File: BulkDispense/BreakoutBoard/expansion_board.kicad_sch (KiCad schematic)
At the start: 10 parts, among them J24 Waste 2/2 Media Valve Power, J25 Waste 2/2 Media Valve GND, J26 Waste Line Sensor 1, J27 Waste Line Sensor 2, J28 Waste Bottle Sensor 1, J29 Waste Bottle Sensor 2, J30 Waste 3/2 Media Valve, J31 Waste Vacuum Sensor 1, J32 Waste Vacuum Sensor 2

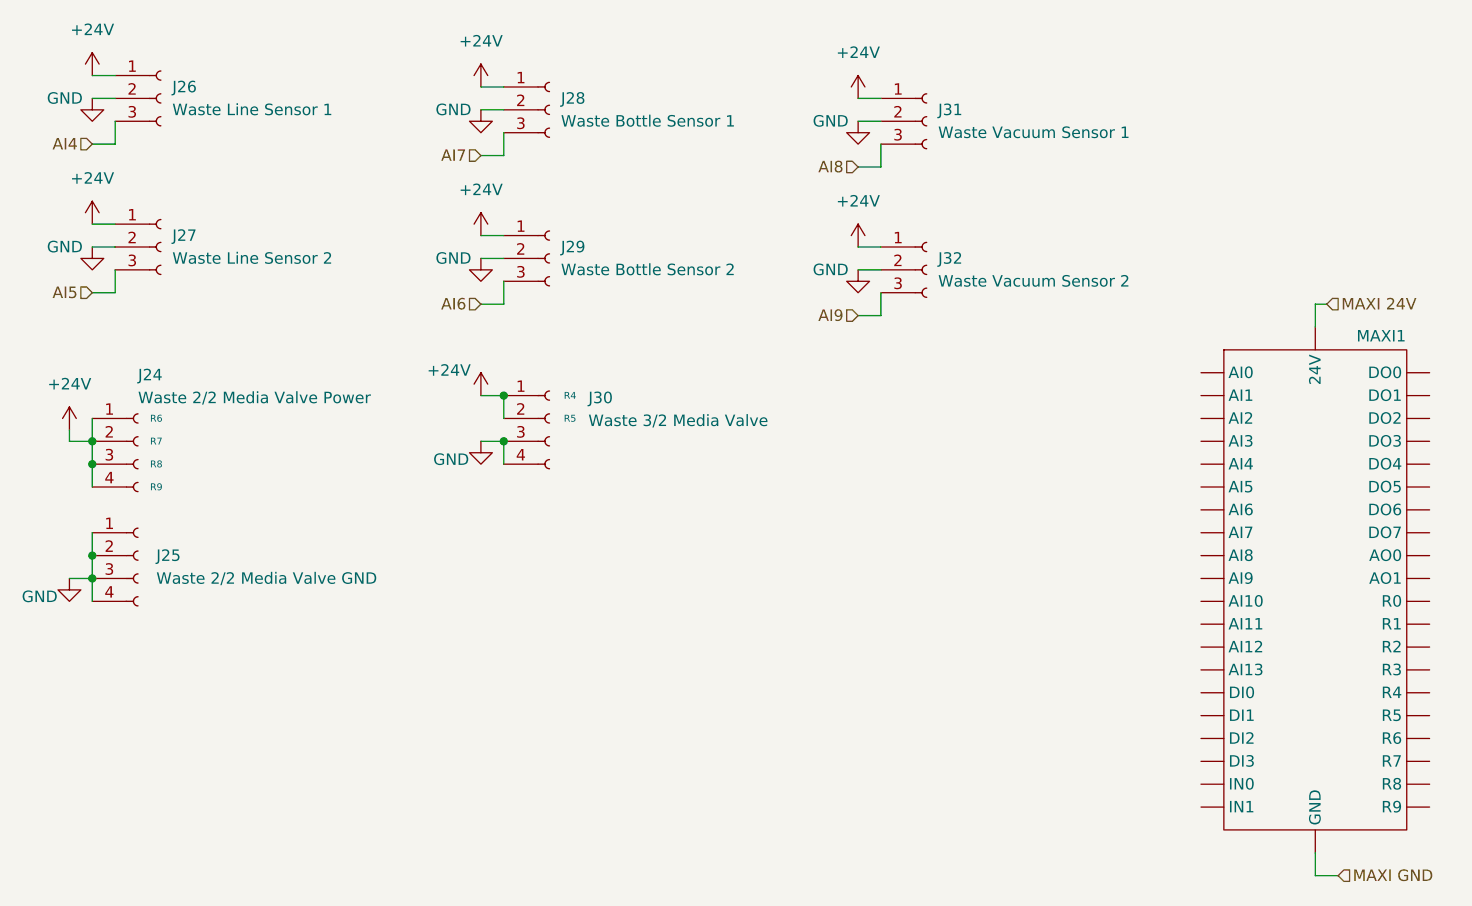
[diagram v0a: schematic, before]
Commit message: Update 3POS Connectors with Mini-Clamp
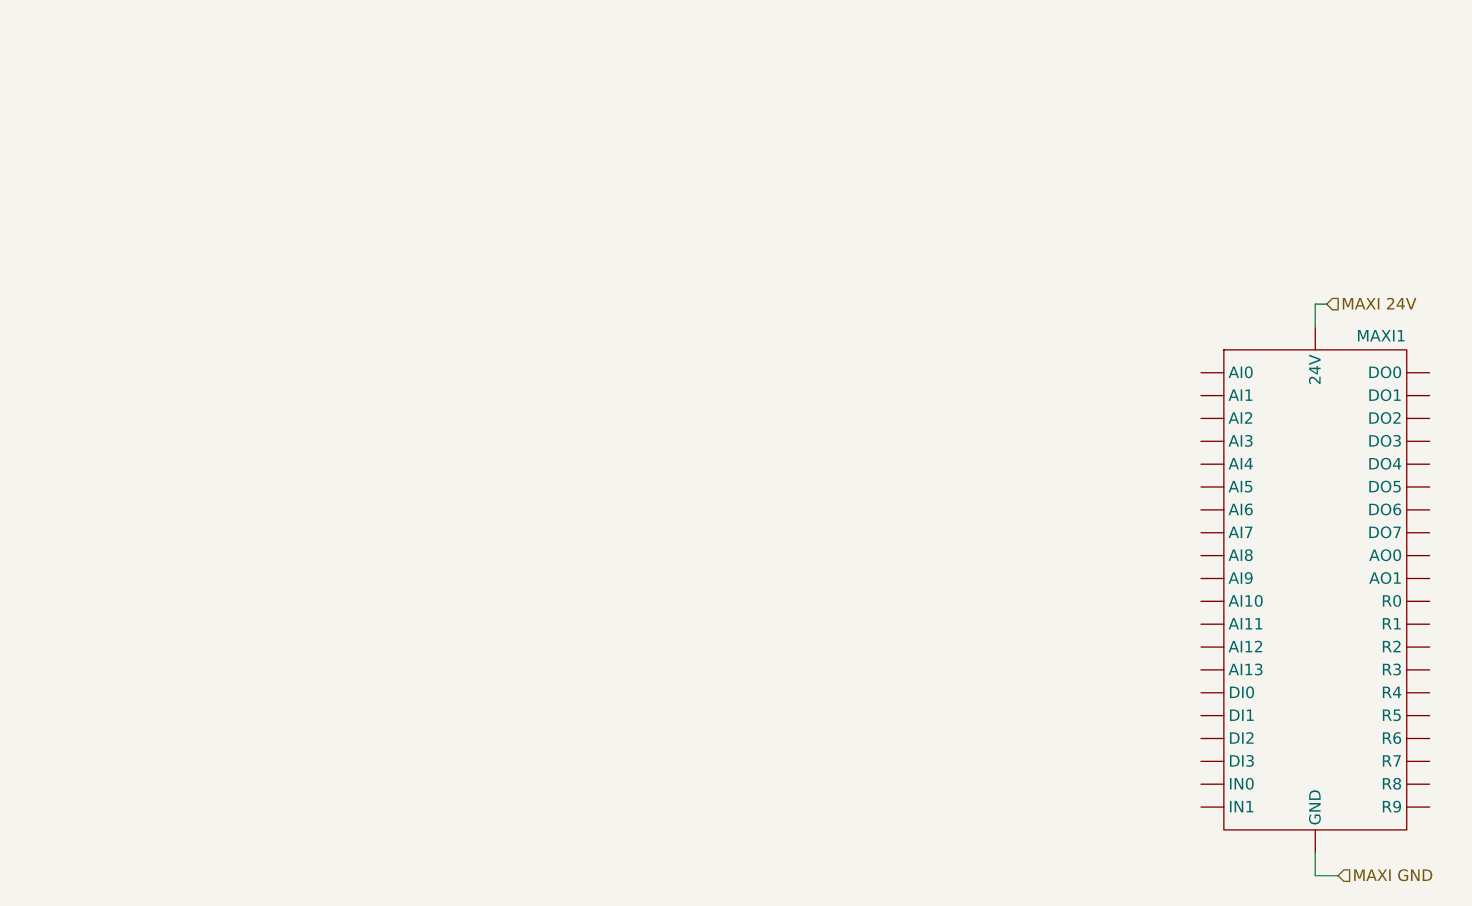
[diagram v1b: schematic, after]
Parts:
- removed J24: Waste 2/2 Media Valve Power, PartsLibrary:CONN04_2165712004_MOL, symbol Connector:Conn_01x04_Socket
- removed J25: Waste 2/2 Media Valve GND, PartsLibrary:CONN04_2165712004_MOL, symbol Connector:Conn_01x04_Socket
- removed J26: Waste Line Sensor 1, PartsLibrary:CONN03_2165711003_MOL, symbol Connector:Conn_01x03_Socket
- removed J27: Waste Line Sensor 2, PartsLibrary:CONN03_2165711003_MOL, symbol Connector:Conn_01x03_Socket
- removed J28: Waste Bottle Sensor 1, PartsLibrary:CONN03_2165711003_MOL, symbol Connector:Conn_01x03_Socket
- removed J29: Waste Bottle Sensor 2, PartsLibrary:CONN03_2165711003_MOL, symbol Connector:Conn_01x03_Socket
- removed J30: Waste 3/2 Media Valve, PartsLibrary:CONN04_2165712004_MOL, symbol Connector:Conn_01x04_Socket
- removed J31: Waste Vacuum Sensor 1, PartsLibrary:CONN03_2165711003_MOL, symbol Connector:Conn_01x03_Socket
- removed J32: Waste Vacuum Sensor 2, PartsLibrary:CONN03_2165711003_MOL, symbol Connector:Conn_01x03_Socket
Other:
- note removed: "R4"
- note removed: "R5"
- note removed: "R6"
- note removed: "R7"
- note removed: "R8"
- note removed: "R9"
